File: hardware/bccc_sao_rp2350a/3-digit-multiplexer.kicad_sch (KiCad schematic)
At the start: 9 parts, among them U201 74HC595D

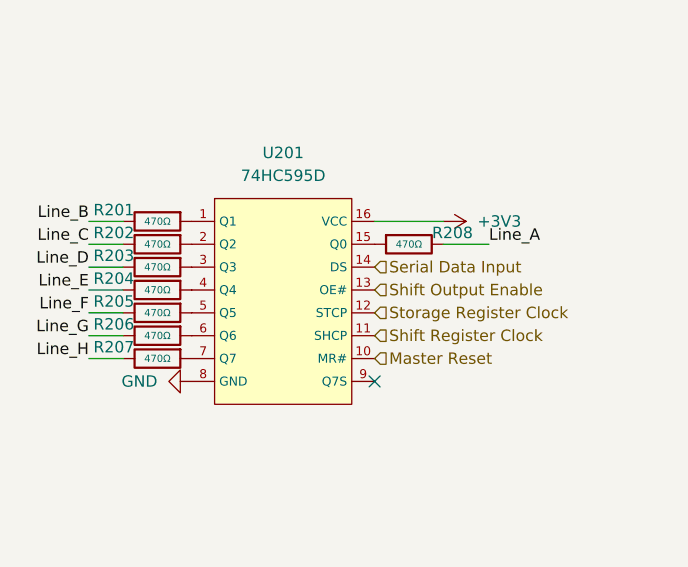
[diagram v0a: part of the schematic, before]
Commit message: hardware edits, changed LED resistor 470->220 ohm, more 'documentation' on board
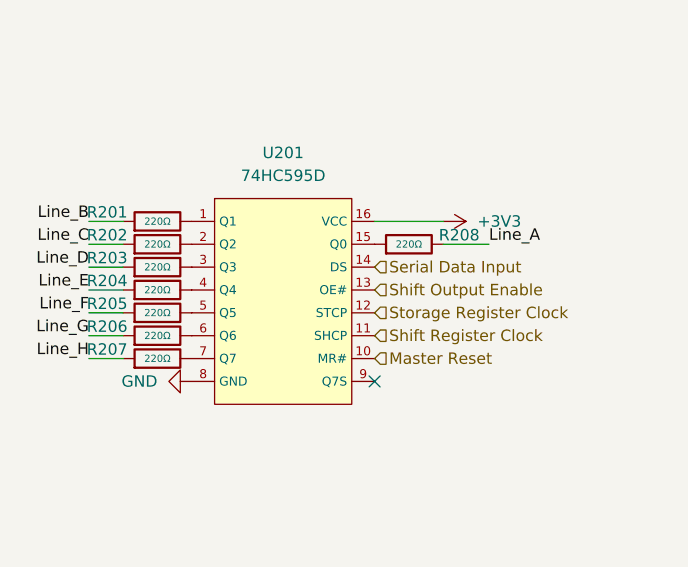
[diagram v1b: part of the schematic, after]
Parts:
- removed R201, R202, R203, R204, R205, R206, R207, R208: 470Ω, PCM_JLCPCB:R_0402, symbol PCM_JLCPCB-Resistors:0402,470Ω
- added R201, R202, R203, R204, R205, R206, R207, R208: 220Ω, PCM_JLCPCB:R_0402, symbol PCM_JLCPCB-Resistors:0402,220Ω
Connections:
- net Line_A: now also R208.2
- net Line_B: now also R201.1
- net Line_C: now also R202.1
- net Line_D: now also R203.1
- net Line_E: now also R204.1
- net Line_F: now also R205.1
- net Line_G: now also R206.1
- net Line_H: now also R207.1
- net at U201.1 (Q1): now also R201.2
- net at U201.15 (Q0): now also R208.1
- net at U201.2 (Q2): now also R202.2
- net at U201.3 (Q3): now also R203.2
- net at U201.4 (Q4): now also R204.2
- net at U201.5 (Q5): now also R205.2
- net at U201.6 (Q6): now also R206.2
- net at U201.7 (Q7): now also R207.2
